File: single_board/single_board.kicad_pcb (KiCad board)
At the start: 4 copper layers, 100 x 100 mm, 126 parts, among them J11 SPI Debug, J17 BOOTSEL, J2 USB_C_Receptacle_USB2.0_16P, J3 SWD, J30 JST_GH_H, J31 JST_GH_H, J33 JST_GH_H, J34 PB_Vertical, J35 JST_GH_H, J36 JST_GH_H, J37 JST_GH_H, J38 PB_Vertical, J39 PB_Vertical, J40 PB_Vertical, J41 PB_Vertical, J42 PB_Vertical, J43 PB_Vertical, J44 PB_Vertical, J45 PB_Vertical, J46 PB_Vertical, J47 PB_Vertical, J48 PB_Vertical, J49 PB_Vertical, J5 JST-GH, J50 PB_Vertical, J53 PB_Vertical, J55 PB_Vertical, J56 Power, J57 PB_Vertical, J6 JST-GH, Q1 AO3400A, Q3 AO3401A, SW1 Button, U1 AP2112K-3.3, U3 USBLC6-2SC6, U4 LSM6DSV, U5 STM32G474VBTx, Y2 ABM8-16MHz

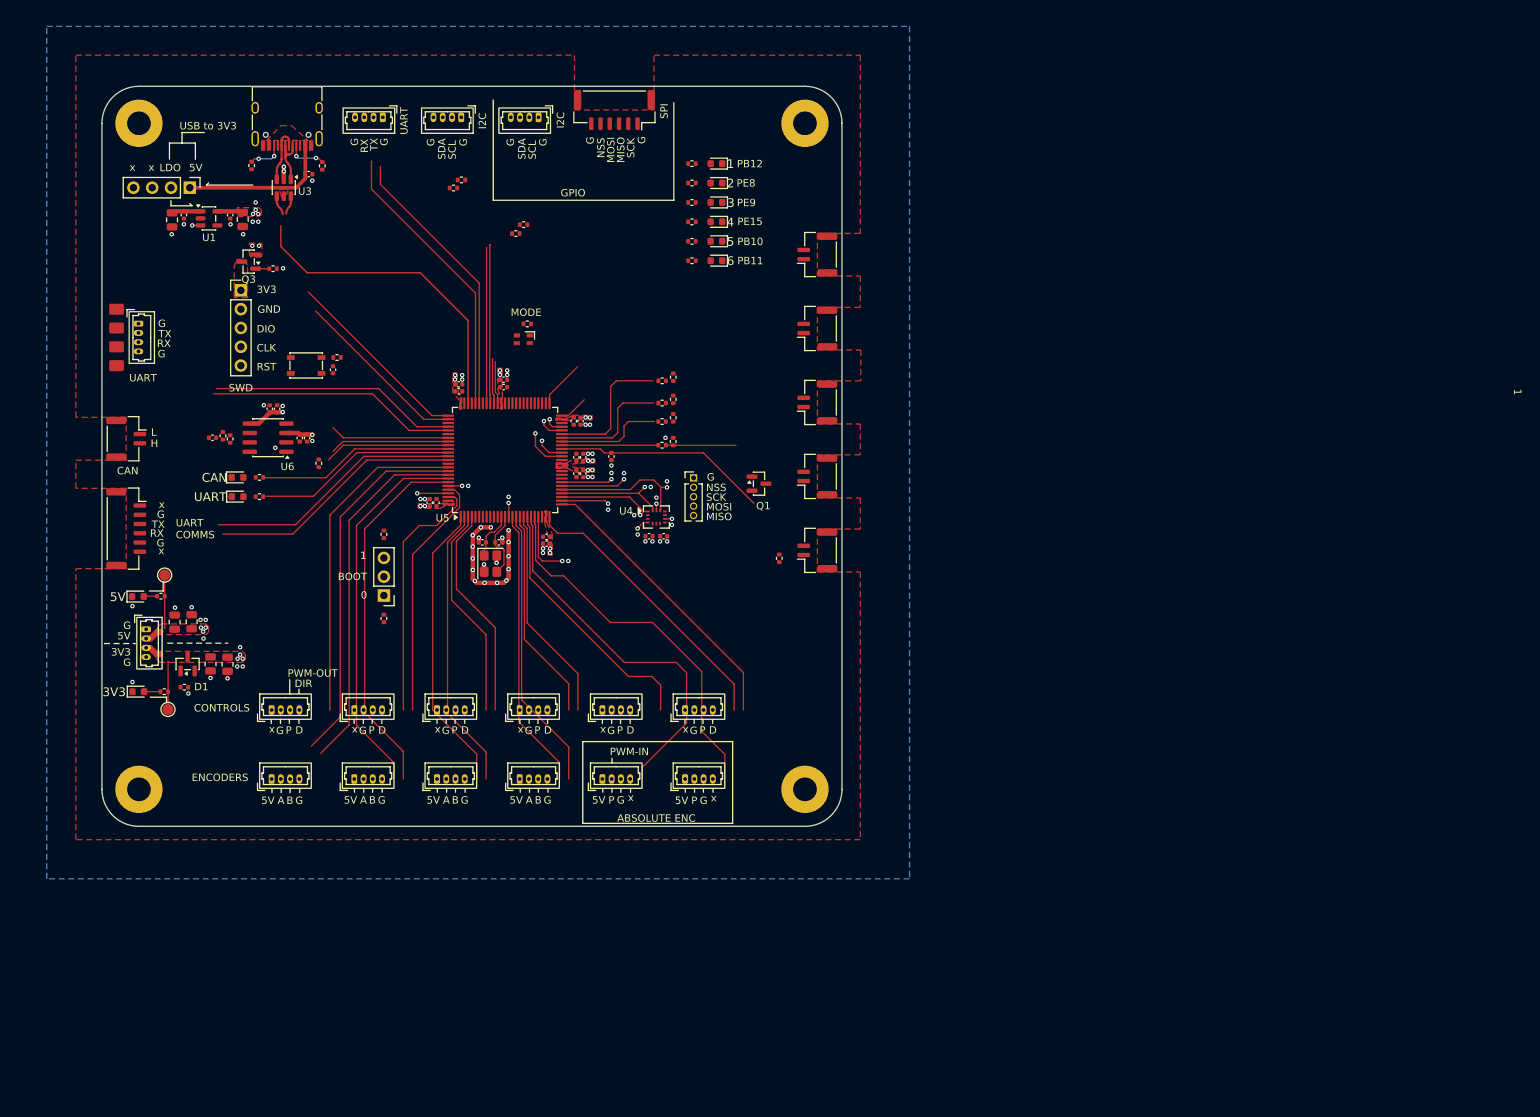
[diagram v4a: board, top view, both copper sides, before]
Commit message: Routing I2C
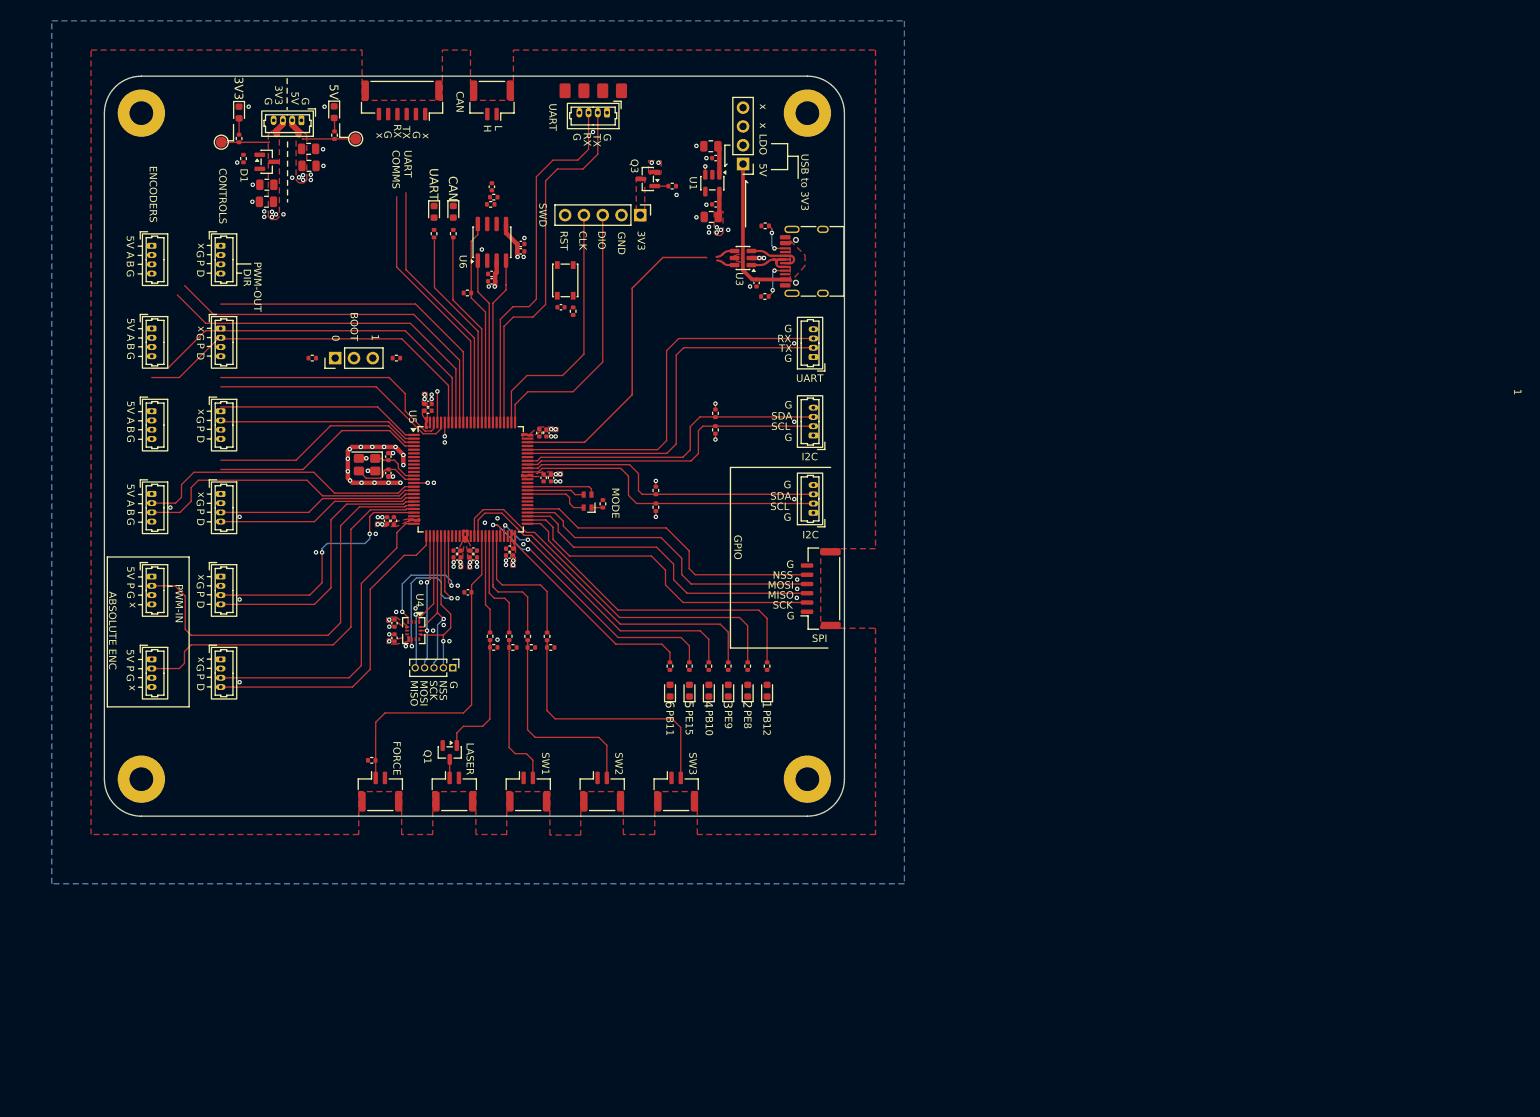
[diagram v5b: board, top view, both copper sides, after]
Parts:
- moved H1 91.4 mm to (52.4, 31.4), turned to 0 degrees
- moved H3 90.3 mm to (142.4, 31.4), turned to 0 degrees
- moved H2 89.7 mm to (52.4, 121.3), turned to 0 degrees
- moved H4 88.6 mm to (142.4, 121.3), turned to 0 degrees
- moved D4 79.4 mm to (65.6, 31.3), turned to -90 degrees
- moved TP2 77.0 mm to (63.2, 35.3), turned to -90 degrees
- moved R15 75.4 mm to (65.6, 34.8), turned to 90 degrees
- moved J33 75.0 mm to (124.6, 123.0), turned to 0 degrees
- moved J56 74.8 mm to (133.7, 38.2), turned to 180 degrees
- moved J2 74.0 mm to (143.4, 51.4), turned to 90 degrees
- moved J43 73.9 mm to (53.8, 105.2), turned to -90 degrees
- moved J39 73.8 mm to (53.8, 49.3), turned to -90 degrees
- moved J54 73.8 mm to (109.6, 26.3), turned to 0 degrees
- moved C31 73.5 mm to (129.3, 35.8), turned to 180 degrees
- moved C3 72.3 mm to (130.0, 37.4), turned to 180 degrees
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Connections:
- J11 pad 3: /IMU_SCK -> /IMU_MOSI
- J11 pad 4: /IMU_MOSI -> /IMU_SCK
- U5 pad 31: /INT1 -> /INT2
- U5 pad 32: /INT2 -> /INT1
- U5 pad 46: /LED4 -> /LED5
- U5 pad 47: /LED5 -> /LED4
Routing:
- net /LED2: track 5.88 -> 51.3 mm, vias 1 -> 0
- net /SPI2_SCK: track 0.00 -> 44.5 mm
- net /SPI2_MISO: track 0.00 -> 43.9 mm
- net /SPI2_MOSI: track 0.00 -> 43.4 mm
- net /LED3: track 3.72 -> 47.1 mm, vias 1 -> 0
- net /SPI2_NSS: track 0.00 -> 42.9 mm
- net /LED1: track 6.50 -> 44.3 mm
- net /I2C4_SCL: track 5.76 -> 42.3 mm
- net /I2C4_SDA: track 6.11 -> 41.8 mm
- net Net-(J33-Pin_2): track 0.00 -> 35.4 mm
- net /LED5: track 2.46 -> 37.8 mm, vias 1 -> 2
- net /LED4: track 3.26 -> 38.5 mm, vias 1 -> 2
- net Net-(J36-Pin_2): track 0.00 -> 28.1 mm
- net /PWM5: track 8.88 -> 35.2 mm, vias 1 -> 2
- net /LED6: track 3.92 -> 29.4 mm
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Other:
- board text added: "FORCE"
- board text added: "LASER"
- board text added: "SW1"
- board text added: "SW2"
- board text added: "SW3"

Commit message: Encoder Routing
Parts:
- moved R26 0.64 mm to (86.2, 64.4), turned to 90 degrees
- moved R27 0.58 mm to (76.0, 64.5), turned to 90 degrees
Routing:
- net /PWM1: track 4.20 -> 49.4 mm, vias 1 -> 2
- net /BOOT0: track 1.88 -> 19.5 mm, vias 1 -> 0
- net /ENC3_B: track 27.5 -> 40.6 mm
- net /ENC3_A: track 27.7 -> 40.8 mm
- net /USART2_RX: track 34.6 -> 45.8 mm
- net /USART2_TX: track 34.9 -> 45.5 mm
- net /ENC1_A: track 49.7 -> 57.4 mm
- net /ENC1_B: track 49.0 -> 55.6 mm
- net Net-(J17-Pin_3): track 0.00 -> 2.78 mm
- net Net-(J17-Pin_1): track 0.00 -> 2.75 mm
- net /DIR3: track 29.1 -> 26.5 mm
- net /ENC2_A: track 51.4 -> 53.8 mm
- net /INT2: track 26.2 -> 28.5 mm
- net /ENC2_B: track 49.9 -> 52.2 mm
- net /DIR1: track 45.0 -> 47.2 mm
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
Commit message: CAN Diff Pair
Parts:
- moved H2 91.0 mm to (143.3, 121.4), turned to 90 degrees
- moved H1 90.1 mm to (53.4, 121.4), turned to 90 degrees
- moved H4 89.9 mm to (143.3, 31.4), turned to 90 degrees
- moved H3 89.0 mm to (53.4, 31.4), turned to 90 degrees
- moved D4 77.9 mm to (53.3, 108.2), turned to 0 degrees
- moved J33 76.6 mm to (145.0, 49.2), turned to 90 degrees
- moved TP2 75.6 mm to (57.3, 110.6), turned to 0 degrees
- moved J43 74.9 mm to (127.2, 120.0), turned to 0 degrees
- moved R15 74.0 mm to (56.8, 108.2), turned to 180 degrees
- moved J56 73.5 mm to (60.2, 40.1), turned to -90 degrees
- moved J2 73.1 mm to (73.4, 30.4), turned to 180 degrees
- moved J39 72.9 mm to (71.3, 120.0), turned to 0 degrees
- moved D8 72.7 mm to (131.4, 36.9), turned to 180 degrees
- moved J54 72.0 mm to (48.3, 64.2), turned to 90 degrees
- moved C31 72.0 mm to (57.8, 44.5), turned to -90 degrees
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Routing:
- net /USB-DN: track 2.51 -> 51.0 mm
- net /CAN_DP: track 0.00 -> 14.9 mm
- net /CAN_DN: track 0.00 -> 14.9 mm
- net /USB-DP: track 45.7 -> 51.0 mm
- net Net-(C41-Pad1): track 0.00 -> 2.05 mm
- net GND: track 25.6 -> 26.3 mm, vias 102 -> 103
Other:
- board text added: "Absolute encoder position for lower Arm motors"
- board text added: "Drivebase Motors use standard CAN frames"
- board text added: "FDCAN"
- board text added: "Quadrature encoder input A/B : Ch1/Ch2 Reconfig Absolute encoder position PWM Input on Ch1 or Ch2"
- board text added: "SET 1"
- board text added: "SET 2"
- board text added: "SET 3"
- board text added: "SET 4"
- board text removed: "FDCAN/CAN"

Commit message: USB Diff Pair
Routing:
- net /USB-DN: track 51.0 -> 50.2 mm
- net /USB-DP: track 51.0 -> 50.2 mm
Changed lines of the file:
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@@
 	)
 	(segment
-		(start 97.825 69.245003)
-		(end 97.825 68.045002)
+		(start 97.82975 58.32975)
+		(end 97.82975 57.968394)
 		(width 0.2906)
 		(layer "F.Cu")
@@
 	)
 	(segment
-		(start 97.82975 68.040252)
-		(end 97.82975 54.89525)
+		(start 97.82975 57.968394)
+		(end 97.82975 57.908573)
+		(width 0.2906)
+		(layer "F.Cu")
+		(net "/USB-DP")
+	)
+	(segment
+		(start 72.495977 42.895976)
+		(end 72.2 42.6)
 		(width 0.2906)
 		(layer "F.Cu")
@@
 	)
 	(segment
-		(start 72.70475 54.89525)
+		(start 97.825 69.245003)
+		(end 97.825 68.045002)
+		(width 0.2906)
+		(layer "F.Cu")
+		(net "/USB-DP")
+	)
+	(segment
+		(start 97.82975 68.040252)
+		(end 97.82975 58.32975)
+		(width 0.2906)
+		(layer "F.Cu")
+		(net "/USB-DP")
+	)
+	(segment
+		(start 72.70475 51.25475)
 		(end 72.70475 43.4)
 		(width 0.2906)
@@
 	)
 	(segment
-		(start 97.82975 54.89525)
-		(end 72.70475 54.89525)
+		(start 94.816421 54.89525)
+		(end 76.34525 54.89525)
 		(width 0.2906)
 		(layer "F.Cu")
@@
 	)
 	(segment
-		(start 98.325 69.245003)
-		(end 98.325 68.045002)
+		(start 71.975 42.056802)
+		(end 71.975 41.264729)
+		(width 0.2906)
+		(layer "F.Cu")
+		(net "/USB-DP")
+	)
+	(arc
+		(start 72.70475 43.4)
+		(mid 72.650492 43.127224)
+		(end 72.495977 42.895976)
+		(width 0.2906)
+		(layer "F.Cu")
+		(net "/USB-DP")
+	)
+	(arc
+		(start 72.2 42.6)
+		(mid 72.033475 42.350779)
+		(end 71.975 42.056802)
+		(width 0.2906)
+		(layer "F.Cu")
+		(net "/USB-DP")
+	)
+	(arc
+		(start 97.82975 57.908573)
+		(mid 96.947164 55.777832)
+		(end 94.816421 54.89525)
+		(width 0.2906)
+		(layer "F.Cu")
+		(net "/USB-DP")
+	)
+	(arc
+		(start 72.70475 51.25475)
+		(mid 73.771028 53.828972)
+		(end 76.34525 54.89525)
+		(width 0.2906)
+		(layer "F.Cu")
+		(net "/USB-DP")
+	)
+	(segment
+		(start 98.32025 68.040252)
+		(end 98.32025 57.890582)
 		(width 0.2906)
 		(layer "F.Cu")
@@
 	)
 	(segment
-		(start 98.32025 54.40475)
-		(end 73.19525 54.40475)
+		(start 73.439379 42.810622)
+		(end 73.65 42.6)
+		(width 0.2906)
+		(layer "F.Cu")
+		(net "/USB-DN")
+	)
+	(segment
+		(start 73.875 42.056802)
+		(end 73.875 41.264729)
+		(width 0.2906)
+		(layer "F.Cu")
+		(net "/USB-DN")
+	)
+	(segment
+		(start 76.60475 54.40475)
+		(end 76.410223 54.404753)
+		(width 0.2906)
+		(layer "F.Cu")
+		(net "/USB-DN")
+	)
+	(segment
+		(start 98.325 69.245003)
+		(end 98.325 68.045002)
 		(width 0.2906)
 		(layer "F.Cu")
@@
 	)
 	(segment
-		(start 98.32025 68.040252)
-		(end 98.32025 54.40475)
+		(start 94.834404 54.40475)
+		(end 76.60475 54.40475)
 		(width 0.2906)
 		(layer "F.Cu")
@@
 	)
 	(segment
-		(start 73.19525 54.40475)
+		(start 73.19525 51.189827)
 		(end 73.19525 43.4)
 		(width 0.2906)
 		(layer "F.Cu")
+		(net "/USB-DN")
+	)
+	(arc
+		(start 98.32025 57.890582)
+		(mid 97.299263 55.425724)
+		(end 94.834404 54.40475)
+		(width 0.2906)
+		(layer "F.Cu")
+		(net "/USB-DN")
+	)
+	(arc
+		(start 76.410223 54.404753)
+		(mid 74.136897 53.46314)
+		(end 73.19525 51.189827)
+		(width 0.2906)
+		(layer "F.Cu")
+		(net "/USB-DN")
+	)
+	(arc
+		(start 73.19525 43.4)
+		(mid 73.258697 43.081031)
+		(end 73.439379 42.810622)
+		(width 0.2906)
+		(layer "F.Cu")
+		(net "/USB-DN")
+	)
+	(arc
+		(start 73.65 42.6)
+		(mid 73.816525 42.350779)
+		(end 73.875 42.056802)
+		(width 0.2906)
+		(layer "F.Cu")
